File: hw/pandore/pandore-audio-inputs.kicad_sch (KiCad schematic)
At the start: 2 parts, among them P4 XLR+TRS6.35+SW, P5 XLR+TRS6.35+SW

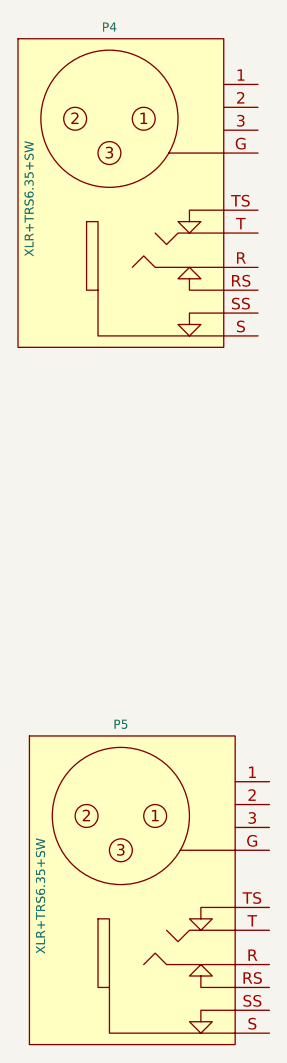
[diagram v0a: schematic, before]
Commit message: added all remaining connectors (only missing M.2 now)
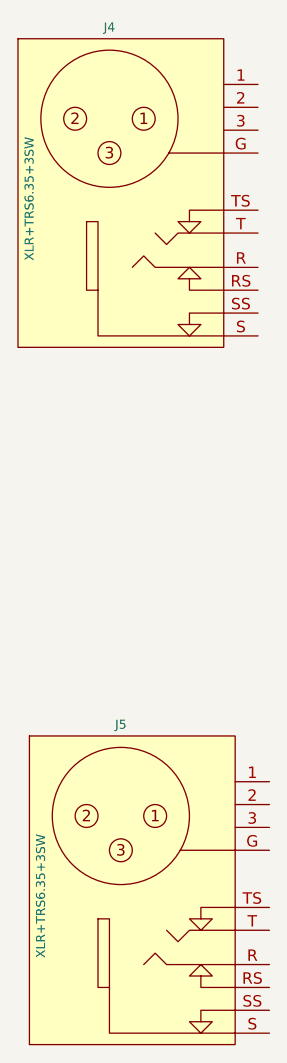
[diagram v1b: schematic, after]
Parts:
- J4: renamed from P4; value XLR+TRS6.35+SW -> XLR+TRS6.35+3SW; symbol reekilib_con:xlr_trs_combo -> reekilib_con:xlr3_trs3sw_combo
- J5: renamed from P5; value XLR+TRS6.35+SW -> XLR+TRS6.35+3SW; symbol reekilib_con:xlr_trs_combo -> reekilib_con:xlr3_trs3sw_combo
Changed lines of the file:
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@@
 	)
 	(symbol
-		(lib_id "reekilib_con:xlr_trs_combo")
+		(lib_id "reekilib_con:xlr3_trs3sw_combo")
 		(at 50.8 45.72 0)
 		(unit 1)
@@
 		(dnp no)
 		(fields_autoplaced yes)
-		(property "Reference" "P4"
+		(property "Reference" "J4"
 			(at 50.8 26.67 0)
 			(do_not_autoplace yes)
@@
 			)
 		)
-		(property "Value" "XLR+TRS6.35+SW"
+		(property "Value" "XLR+TRS6.35+3SW"
 			(at 41.91 45.72 90)
 			(do_not_autoplace yes)
@@
 			)
 		)
-		(property "Description" "XLR TRS6.35mm combo receptacle with all switches"
+		(property "Description" "XLR TRS6.35mm combo receptacle with 3 switches"
 			(at 50.8 70.485 0)
 			(do_not_autoplace yes)
@@
 			(project ""
 				(path "/e55f2700-f75a-4062-8a27-fe258faa8966/b4e2772d-7748-46ec-bd38-bc8e72cebcb8/505def28-a163-4964-82bd-abe7e8697de4"
-					(reference "P4")
+					(reference "J4")
+					(unit 1)
+				)
+				(path "/e55f2700-f75a-4062-8a27-fe258faa8966/b4e2772d-7748-46ec-bd38-bc8e72cebcb8/9a4ddd59-6699-41a4-a382-0b3d520d6256"
+					(reference "P6")
 					(unit 1)
 				)
@@
 	)
 	(symbol
-		(lib_id "reekilib_con:xlr_trs_combo")
+		(lib_id "reekilib_con:xlr3_trs3sw_combo")
 		(at 52.07 123.19 0)
 		(unit 1)
@@
 		(dnp no)
 		(fields_autoplaced yes)
-		(property "Reference" "P5"
+		(property "Reference" "J5"
 			(at 52.07 104.14 0)
 			(do_not_autoplace yes)
@@
 			)
 		)
-		(property "Value" "XLR+TRS6.35+SW"
+		(property "Value" "XLR+TRS6.35+3SW"
 			(at 43.18 123.19 90)
 			(do_not_autoplace yes)
@@
 			)
 		)
-		(property "Description" "XLR TRS6.35mm combo receptacle with all switches"
+		(property "Description" "XLR TRS6.35mm combo receptacle with 3 switches"
 			(at 52.07 147.955 0)
 			(do_not_autoplace yes)
@@
 			(project "pandore"
 				(path "/e55f2700-f75a-4062-8a27-fe258faa8966/b4e2772d-7748-46ec-bd38-bc8e72cebcb8/505def28-a163-4964-82bd-abe7e8697de4"
-					(reference "P5")
-					(unit 1)
-				)
+					(reference "J5")
+					(unit 1)
+				)
+				(path "/e55f2700-f75a-4062-8a27-fe258faa8966/b4e2772d-7748-46ec-bd38-bc8e72cebcb8/9a4ddd59-6699-41a4-a382-0b3d520d6256"
+					(reference "P7")
+					(unit 1)
+				)

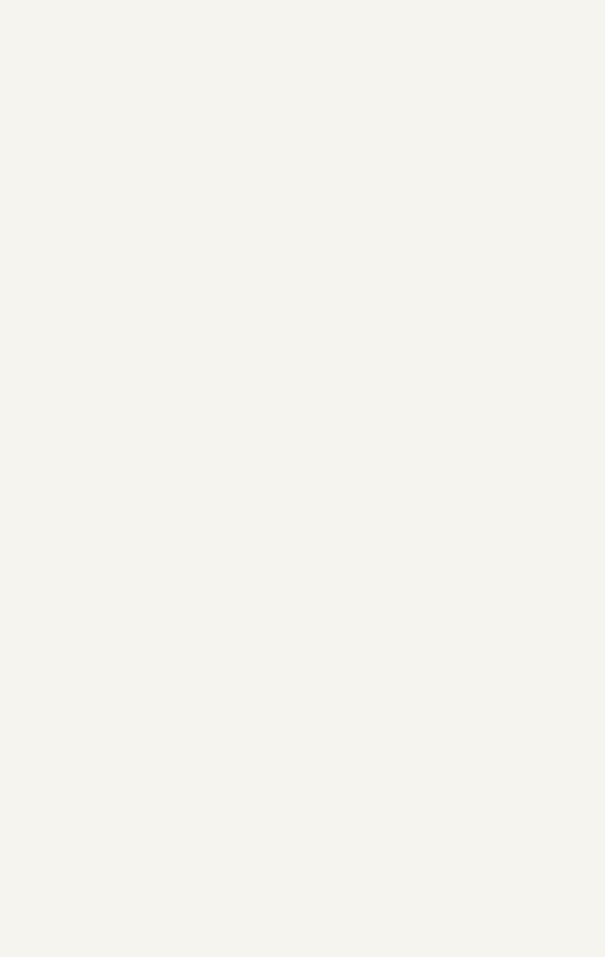
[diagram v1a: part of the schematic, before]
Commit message: Added lots to sch and pcb: eth passive, audio codec, midi, teensy Corrected and added support for M.2
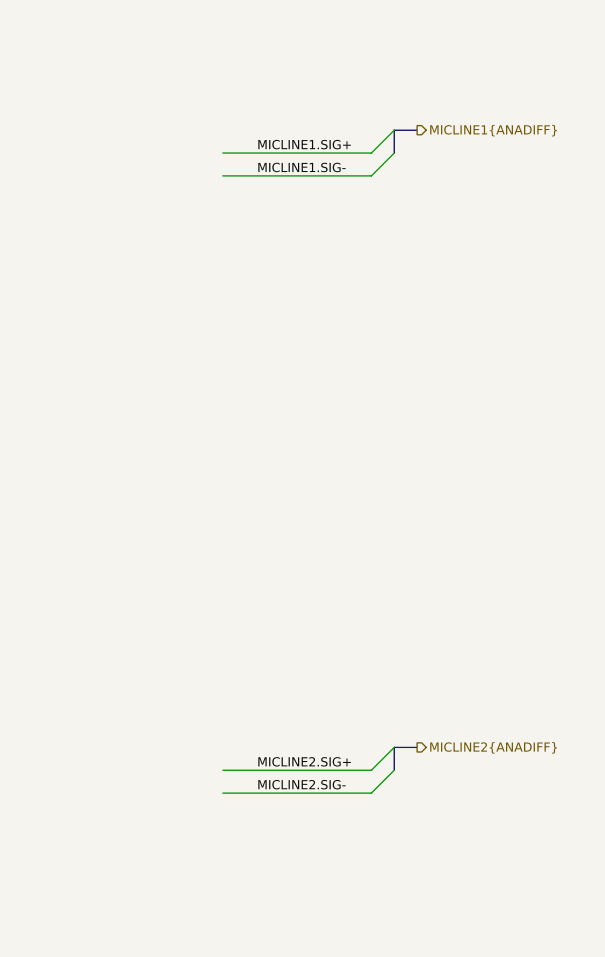
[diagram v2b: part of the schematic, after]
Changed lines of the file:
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@@
 		(company "${corp}")
+	)
+	(bus_entry
+		(at 251.46 38.1)
+		(size -2.54 2.54)
+		(stroke
+			(width 0)
+			(type default)
+		)
+	)
+	(bus_entry
+		(at 251.46 40.64)
+		(size -2.54 2.54)
+		(stroke
+			(width 0)
+			(type default)
+		)
+	)
+	(bus_entry
+		(at 251.46 109.22)
+		(size -2.54 2.54)
+		(stroke
+			(width 0)
+			(type default)
+		)
+	)
+	(bus_entry
+		(at 251.46 106.68)
+		(size -2.54 2.54)
+		(stroke
+			(width 0)
+			(type default)
+		)
+	)
+	(wire
+		(pts
+			(xy 232.41 109.22) (xy 248.92 109.22)
+		)
+		(stroke
+			(width 0)
+			(type default)
+		)
+	)
+	(wire
+		(pts
+			(xy 232.41 43.18) (xy 248.92 43.18)
+		)
+		(stroke
+			(width 0)
+			(type default)
+		)
+	)
+	(bus
+		(pts
+			(xy 254 106.68) (xy 251.46 106.68)
+		)
+		(stroke
+			(width 0)
+			(type default)
+		)
+	)
+	(wire
+		(pts
+			(xy 232.41 111.76) (xy 248.92 111.76)
+		)
+		(stroke
+			(width 0)
+			(type default)
+		)
+	)
+	(bus
+		(pts
+			(xy 251.46 38.1) (xy 251.46 40.64)
+		)
+		(stroke
+			(width 0)
+			(type default)
+		)
+	)
+	(bus
+		(pts
+			(xy 254 38.1) (xy 251.46 38.1)
+		)
+		(stroke
+			(width 0)
+			(type default)
+		)
+	)
+	(wire
+		(pts
+			(xy 232.41 40.64) (xy 248.92 40.64)
+		)
+		(stroke
+			(width 0)
+			(type default)
+		)
+	)
+	(bus
+		(pts
+			(xy 251.46 106.68) (xy 251.46 109.22)
+		)
+		(stroke
+			(width 0)
+			(type default)
+		)
+	)
+	(label "MICLINE2.SIG-"
+		(at 236.22 111.76 0)
+		(effects
+			(font
+				(size 1.016 1.016)
+			)
+			(justify left bottom)
+		)
+	)
+	(label "MICLINE2.SIG+"
+		(at 236.22 109.22 0)
+		(effects
+			(font
+				(size 1.016 1.016)
+			)
+			(justify left bottom)
+		)
+	)
+	(label "MICLINE1.SIG+"
+		(at 236.22 40.64 0)
+		(effects
+			(font
+				(size 1.016 1.016)
+			)
+			(justify left bottom)
+		)
+	)
+	(label "MICLINE1.SIG-"
+		(at 236.22 43.18 0)
+		(effects
+			(font
+				(size 1.016 1.016)
+			)
+			(justify left bottom)
+		)
+	)
+	(hierarchical_label "MICLINE2{ANADIFF}"
+		(shape output)
+		(at 254 106.68 0)
+		(effects
+			(font
+				(size 1.016 1.016)
+			)
+			(justify left)
+		)
+	)
+	(hierarchical_label "MICLINE1{ANADIFF}"
+		(shape output)
+		(at 254 38.1 0)
+		(effects
+			(font
+				(size 1.016 1.016)
+			)
+			(justify left)
+		)
 	)
 	(symbol
@@
 					(unit 1)
 				)
-				(path "/e55f2700-f75a-4062-8a27-fe258faa8966/b4e2772d-7748-46ec-bd38-bc8e72cebcb8/9a4ddd59-6699-41a4-a382-0b3d520d6256"
-					(reference "P6")
-					(unit 1)
-				)
 			)
 		)
@@
 					(unit 1)
 				)
-				(path "/e55f2700-f75a-4062-8a27-fe258faa8966/b4e2772d-7748-46ec-bd38-bc8e72cebcb8/9a4ddd59-6699-41a4-a382-0b3d520d6256"
-					(reference "P7")
-					(unit 1)
-				)

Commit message: lots of work done all around
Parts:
- added C139, C146, C147, C158, C167, C168, C169, C170, C171, C172: ${Capacitance}, ${Voltage}, ${Dielectric}, reekilib_cap:CAPC1608, symbol reekilib_cap:cap
- added C159, C160, C161, C162, C163, C164, C165, C166: ${Capacitance}, ${Voltage}, ${Tolerance}, reekilib_cap:CAPAE630Xxxx, symbol reekilib_cap:cap_pol
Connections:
- net AVSS: now reaches J4.1
- net AVSS: now also J4.G, J4.S, J5.1, J5.G, J5.S, C139.2, C146.2, C147.1, C158.1, C169.1, C171.1
- net _MIC1IN.SIG+: now reaches J4.2
- net _MIC1IN.SIG+: now also C139.1, C163.1 (+)
- net _MIC1IN.SIG-: now reaches J4.3
- net _MIC1IN.SIG-: now also C158.2, C164.1 (+)
- net _LINE1IN.SIG-: now reaches J4.R
- net _LINE1IN.SIG-: now also C160.1 (+), C170.2
- net _LINE1IN.SIG+: now reaches J4.T
- net _LINE1IN.SIG+: now also C159.1 (+), C172.2
- net _MIC2IN.SIG+: now reaches J5.2
- net _MIC2IN.SIG+: now also C146.1, C165.1 (+)
- net _MIC2IN.SIG-: now reaches J5.3
- net _MIC2IN.SIG-: now also C147.2, C166.1 (+)
- net _LINE2IN.SIG-: now reaches J5.R
- net _LINE2IN.SIG-: now also C162.1 (+), C167.2
- net _LINE2IN.SIG+: now reaches J5.T
- net _LINE2IN.SIG+: now also C161.1 (+), C168.2
- new net: C167.1, C168.1, C169.2
- new net: C170.1, C171.2, C172.1
- new net LINE1IN.SIG+: C159.2 (-)
- new net LINE1IN.SIG-: C160.2 (-)
- new net LINE2IN.SIG+: C161.2 (-)
- new net LINE2IN.SIG-: C162.2 (-)
- new net MIC1IN.SIG+: C163.2 (-)
- new net MIC1IN.SIG-: C164.2 (-)
- new net MIC2IN.SIG+: C165.2 (-)
- new net MIC2IN.SIG-: C166.2 (-)
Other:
- added sheet IN buffer 1 (pandore-audio-inbuf.kicad_sch)
- added sheet IN buffer 2 (pandore-audio-inbuf.kicad_sch)
- moved on the sheet: J4, J5

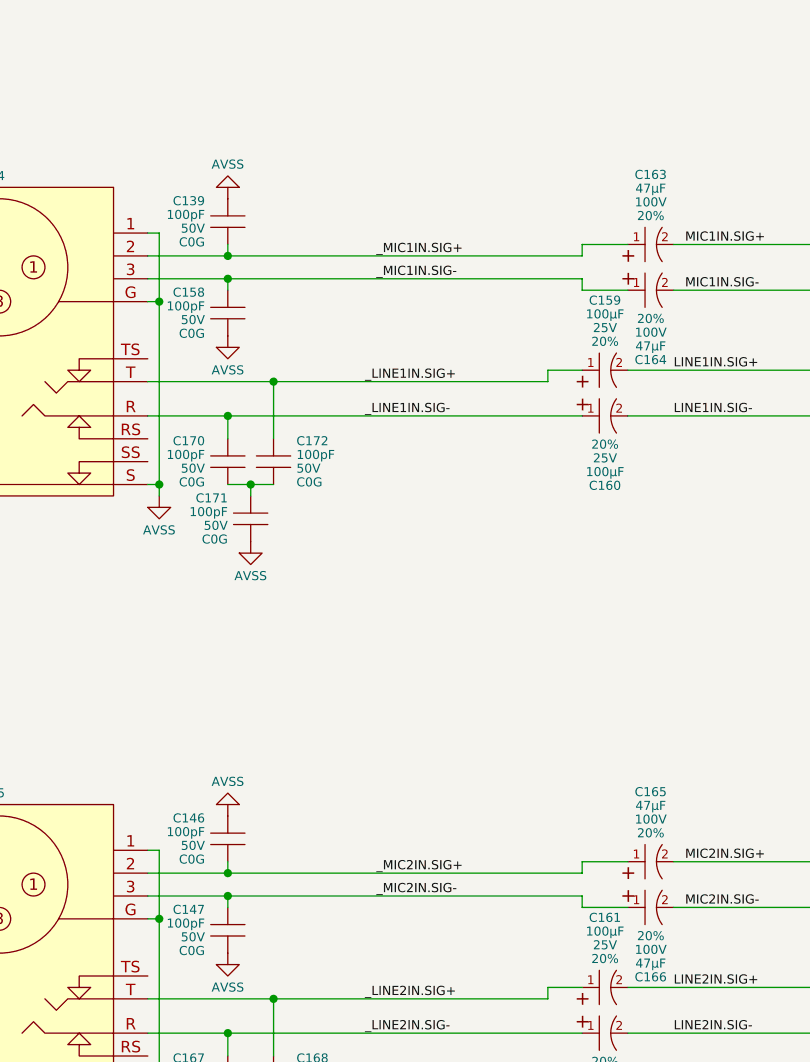
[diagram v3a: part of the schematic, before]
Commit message: lcd control circuit added fan interface added rgba output pinout for management mcu accessories done
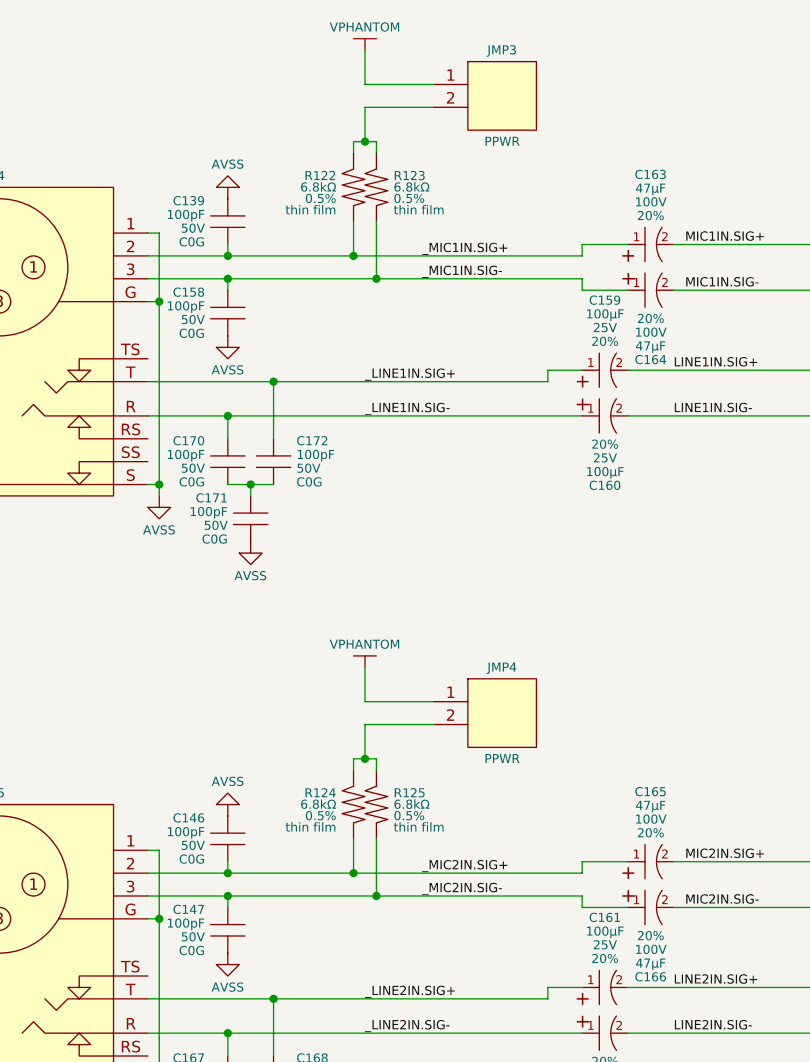
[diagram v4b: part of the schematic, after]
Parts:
- added JMP3, JMP4: PPWR, reekilib_con:HDR254P1X02-TH, symbol reekilib_con:hdr-1x2
- added R122, R123, R124, R125: ${Resistance}, ${Tolerance}, ${Type}, reekilib_res:RESC2012, symbol reekilib_res:res
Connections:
- net _MIC1IN.SIG+: now also R122.1
- net _MIC1IN.SIG-: now also R123.1
- net _MIC2IN.SIG+: now also R124.1
- net _MIC2IN.SIG-: now also R125.1
- new net: JMP4.2, R124.2, R125.2
- new net: JMP3.2, R122.2, R123.2
- new net VPHANTOM: JMP3.1, JMP4.1

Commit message: added todos following review
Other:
- note added: "TODO: report if jack is connected check if XLR is doable easy"
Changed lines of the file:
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@@
 		(company "${corp}")
+	)
+	(text "TODO: report if jack is connected check if XLR is doable easy"
+		(exclude_from_sim no)
+		(at 56.642 157.48 0)
+		(effects
+			(font
+				(size 1.27 1.27)
+			)
+		)
 	)
 	(junction

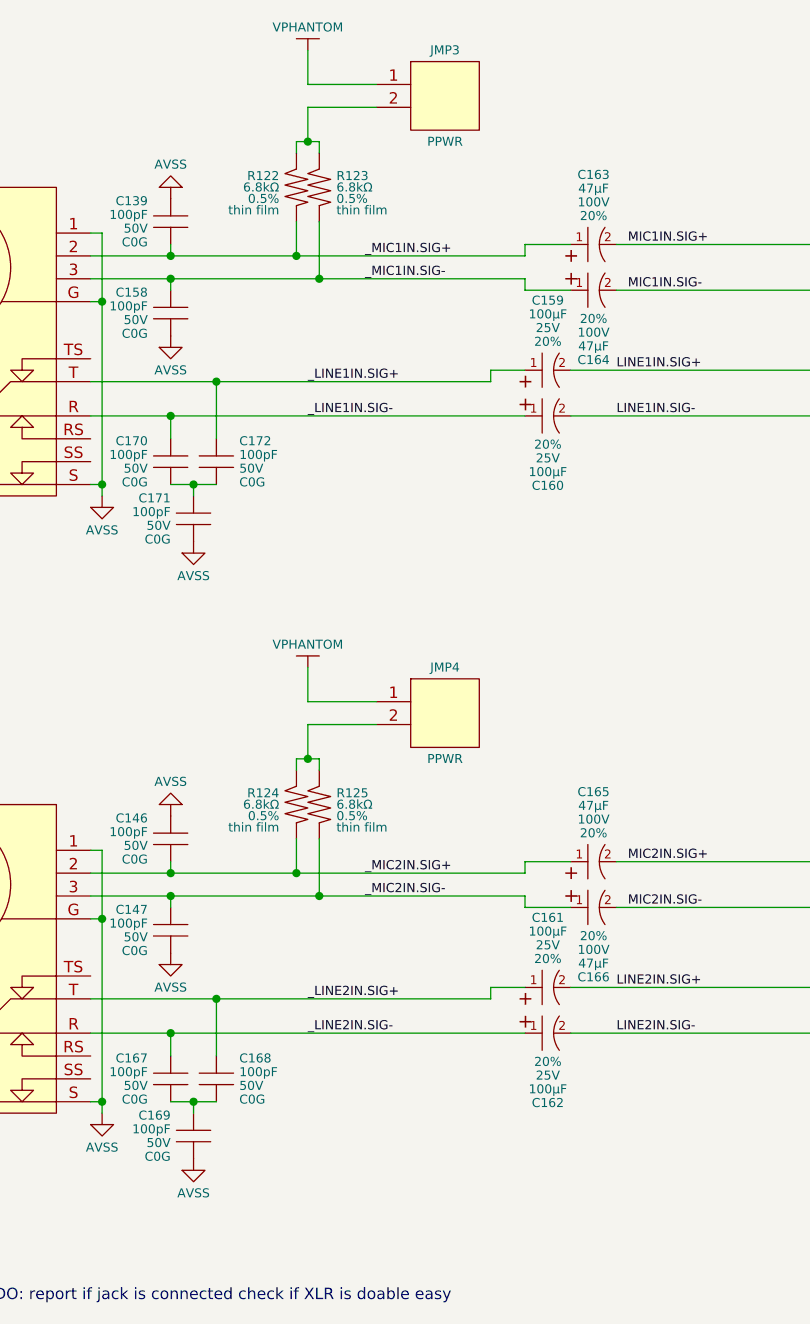
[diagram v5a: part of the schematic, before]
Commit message: added expansion port and more ctl to rp2350s routing much progress
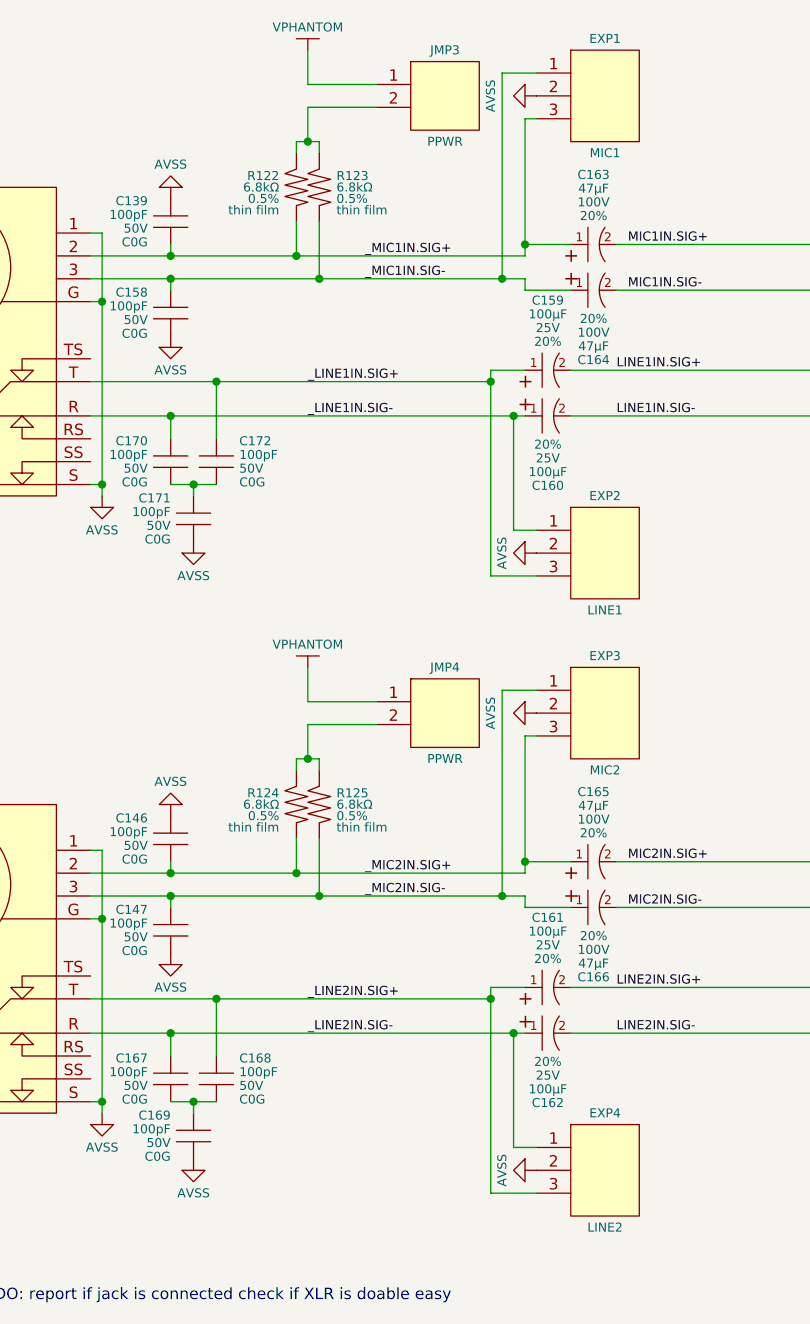
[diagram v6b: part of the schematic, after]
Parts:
- added EXP1: MIC1, reekilib_con:HDR254P1X03-TH, symbol reekilib_con:hdr-1x3
- added EXP2: LINE1, reekilib_con:HDR254P1X03-TH, symbol reekilib_con:hdr-1x3
- added EXP3: MIC2, reekilib_con:HDR254P1X03-TH, symbol reekilib_con:hdr-1x3
- added EXP4: LINE2, reekilib_con:HDR254P1X03-TH, symbol reekilib_con:hdr-1x3
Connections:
- net AVSS: now also EXP1.2, EXP2.2, EXP3.2, EXP4.2
- net _LINE1IN.SIG+: now also EXP2.3
- net _LINE1IN.SIG-: now also EXP2.1
- net _LINE2IN.SIG+: now also EXP4.3
- net _LINE2IN.SIG-: now also EXP4.1
- net _MIC1IN.SIG+: now also EXP1.3
- net _MIC1IN.SIG-: now also EXP1.1
- net _MIC2IN.SIG+: now also EXP3.3
- net _MIC2IN.SIG-: now also EXP3.1
